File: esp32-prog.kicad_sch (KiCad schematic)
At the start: 14 parts

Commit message: draft schematics complete
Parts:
- added C7, C8, C9: 100n_0402_CL05B104KB54PNC, Capacitor_SMD:C_0603_1608Metric, symbol 00-kiml-capacitors-smd:100n_0402_CL05B104KB54PNC
- added D? (x3): 0603_RED_KT-0603R, LED_SMD:LED_0603_1608Metric, symbol 00-kiml-led-smd:0603_RED_KT-0603R
- added J?: 1.27mm_50mils_male_DW127R-22-10-23_02x05, Connector_PinHeader_1.27mm:PinHeader_2x05_P1.27mm_Vertical, symbol 00-kiml-connector-pin-header-1.27mm:1.27mm_50mils_male_DW127R-22-10-23_02x05
- added Q1, Q2: AO3400A, Package_TO_SOT_SMD:SOT-23, symbol 00-kiml-transitor-fet:AO3400A
- added R3, R4, R7, R8, R?: 10k_0402_0402WGF1002TCE, Resistor_SMD:R_0402_1005Metric, symbol 00-kiml-resistors-smd:10k_0402_0402WGF1002TCE
- added R5, R6, R? (x3): 1k_0402_0402WGF1001TCE, Resistor_SMD:R_0402_1005Metric, symbol 00-kiml-resistors-smd:1k_0402_0402WGF1001TCE
- added SW?: SW_DIP_x02_50mil_1.27mm_TP-02, symbol 00-kiml-button-switch-smd:SW_DIP_x02_50mil_1.27mm_TP-02
- added U5, U6, U?: 74LVC1G125GW_Nexperia, Package_TO_SOT_SMD:SOT-23-5, symbol 00-kiml-74xGxx:74LVC1G125GW_Nexperia
- R1, R2: renamed from R?; UserValue 1k -> 10k
- gave numbers to parts that had none: 12
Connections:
- net +5V: now also J?.1 (Pin_1), R?.1, SW?.4; no longer C1.1, L1.2, U1.3 (VI)
- net GND: now also J1.5 (GND), J1.6 (Shield), C7.2, C8.2, C9.2, D?.1 (K), D?.1 (K), D?.1 (K), J?.10 (Pin_10), J?.9 (Pin_9), R3.2, R4.2, R?.2, U5.3 (G), U6.3 (G), U?.3 (G); no longer U2.2 (VN), U2.4 (IO3), U2.6 (IO4)
- net TXD: now reaches U4.4
- net TXD: now also J?.8 (Pin_8)
- net at U3.13 (~{DTR}): now also U5.2
- net at U3.14 (~{RTS}): now also U6.2
- net at U3.3 (RXD): now also U?.4
- net +3V3 renamed +3.3VA
- net +3.3VA: now also SW?.2; no longer U4.5 (V)
- new net: Q1.2 (S), Q2.1 (G), R6.2, R8.2
- new net: R6.1, U6.4
- new net: D?.2 (A), R?.2 (x3)
- new net: R5.1, U5.4
- new net: Q1.1 (G), Q2.2 (S), R5.2, R7.2
- new net: R?.1, U?.1
- new net: R4.1, U6.1
- new net: R3.1, U5.1
- new net: U2.2 (VN), U2.4 (IO3), U2.6 (IO4)
- new net +3.3V: C7.1, C8.1, C9.1, J?.2 (Pin_2), R7.1, R8.1, R?.1, SW?.3, U4.5 (V), U5.5 (V), U6.5 (V), U?.5 (V)
- new net ESP_BOOT: J?.6 (Pin_6), Q2.3 (D)
- new net ESP_EN: J?.5 (Pin_5), Q1.3 (D)
- new net RXD: J?.7 (Pin_7), U?.2
- new net VBUS: C1.1, L1.2, R?.1, SW?.1, U1.3 (VI)
- no-connect marks 0 -> 6
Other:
- note added: "2. Mating wire should pair with https://www.tag-connect.com/product/tc2050-idc-nl-050-all"
- note added: "TODO: LEDs on TX/RX lines to indicate comms?"
- moved on the sheet: C1, C2, C3, C4, C5, C6, L1, R1, R2, U1, U2, U3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

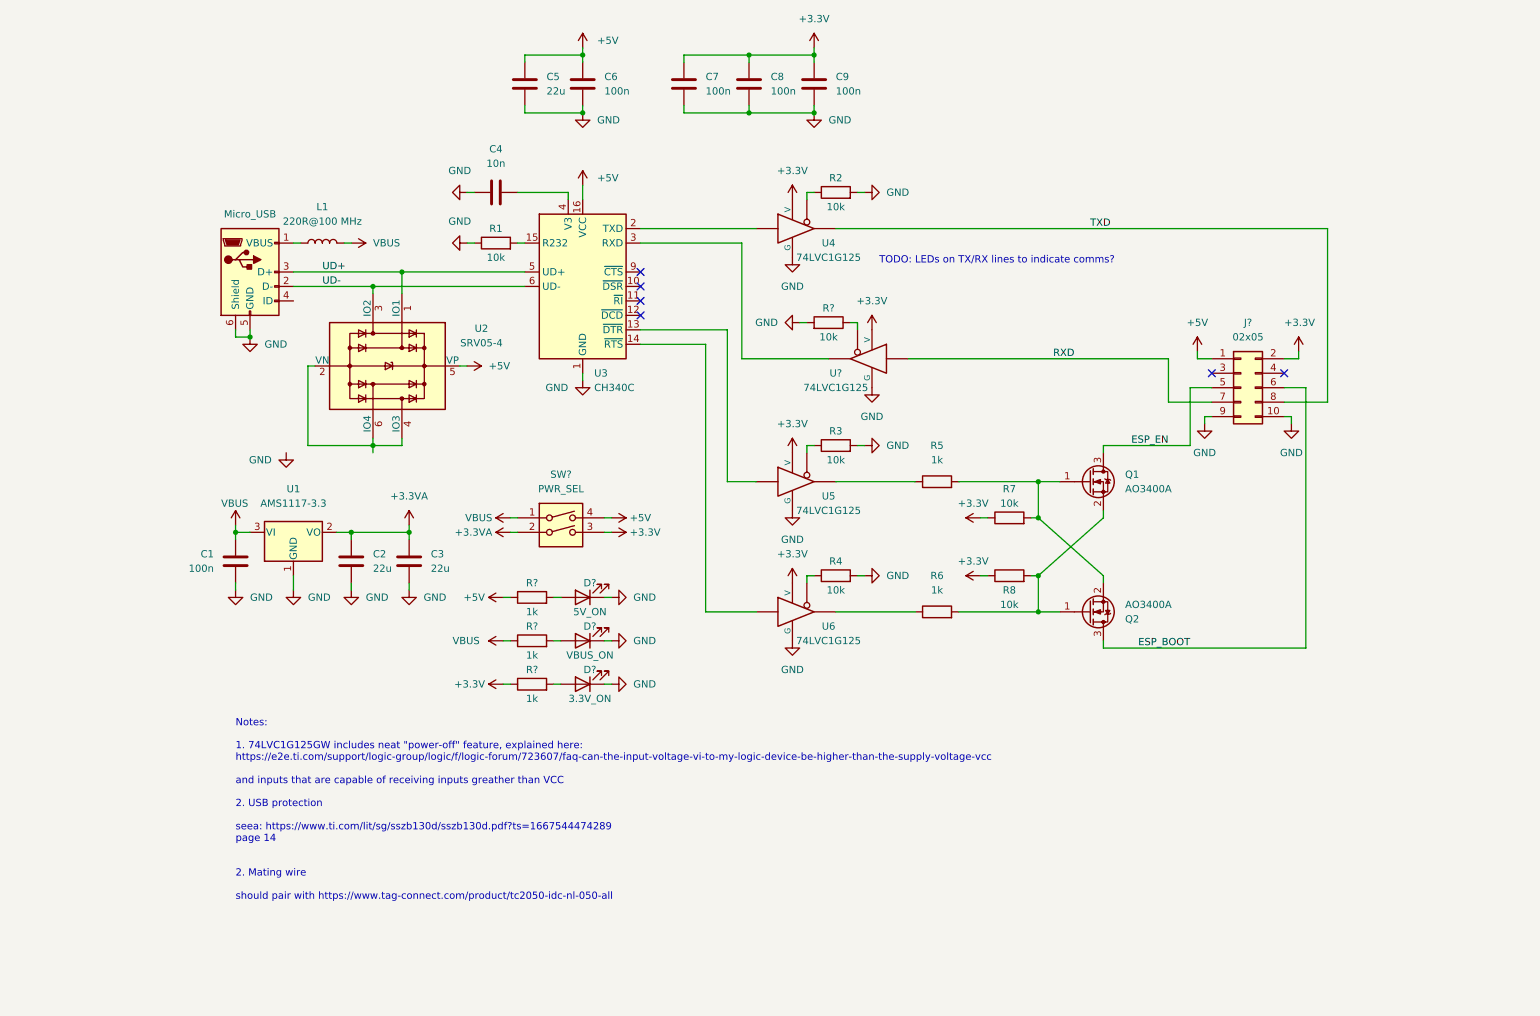
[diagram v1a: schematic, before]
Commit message: fix DRC in schematics
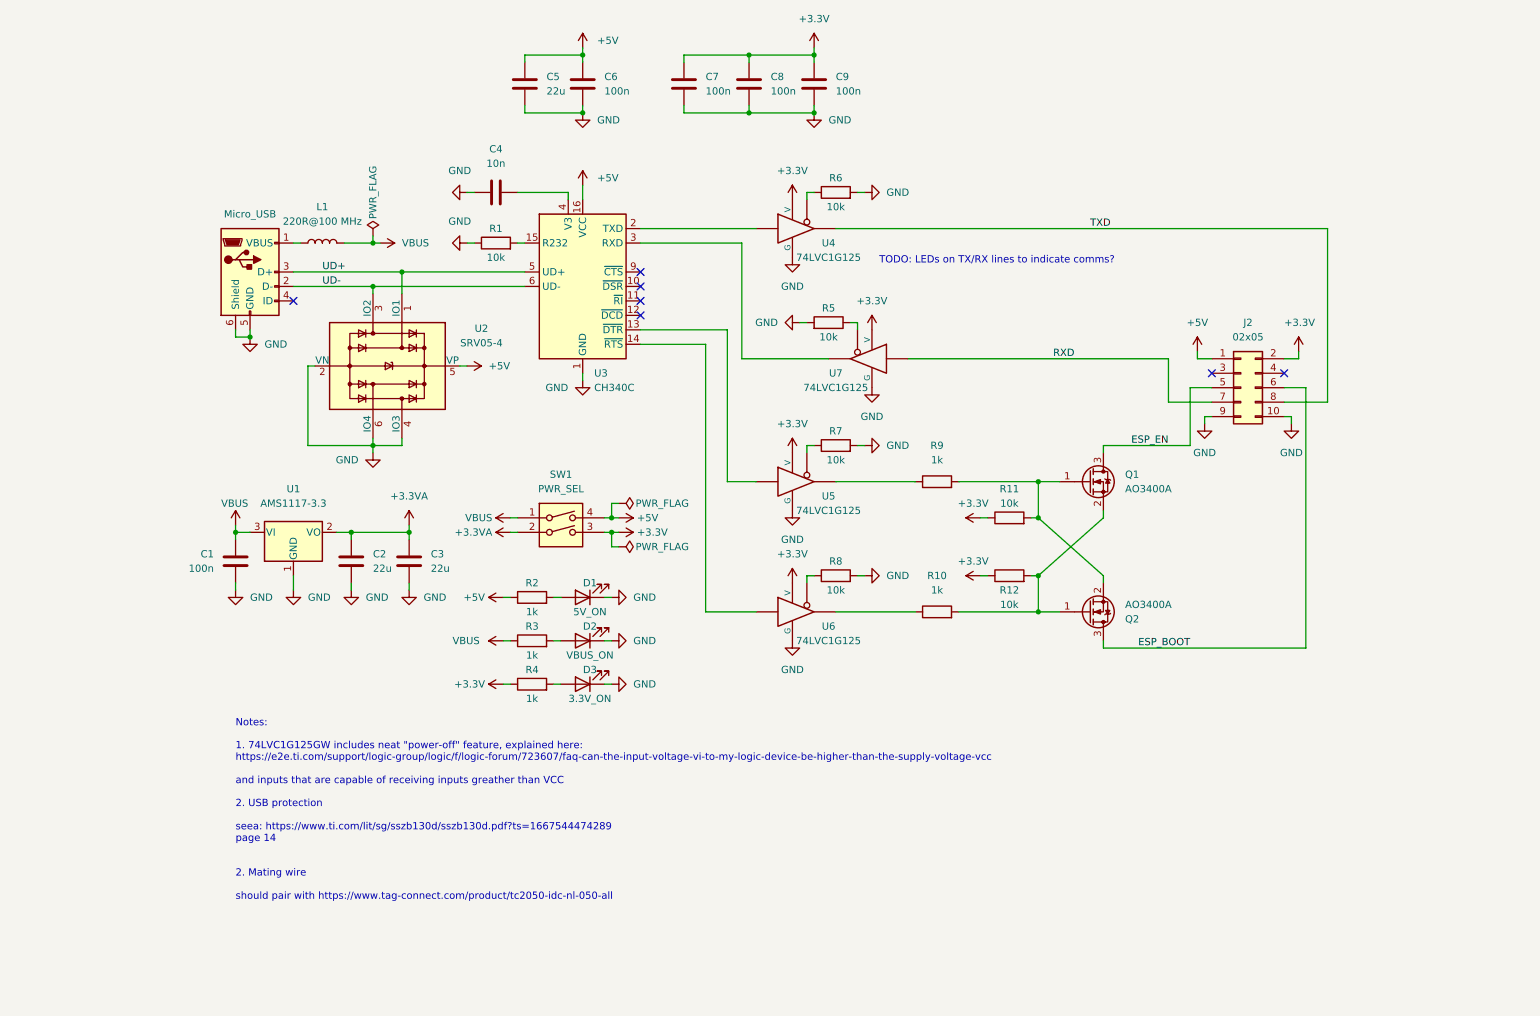
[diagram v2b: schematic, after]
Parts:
- SW1: renamed from SW?; footprint (none) -> 00-kiml-button-switch-smd:SW_DIP_1.27mm_0.50mil_TP-02
- gave numbers to parts that had none: 9
- renumbered R6 to R10, R7 to R11, R8 to R12, R2 to R6, R3 to R7, R4 to R8, R5 to R9
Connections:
- net GND: now also U2.2 (VN), U2.4 (IO3), U2.6 (IO4)
- no-connect marks 6 -> 7

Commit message: begin routing: place all basic blocks
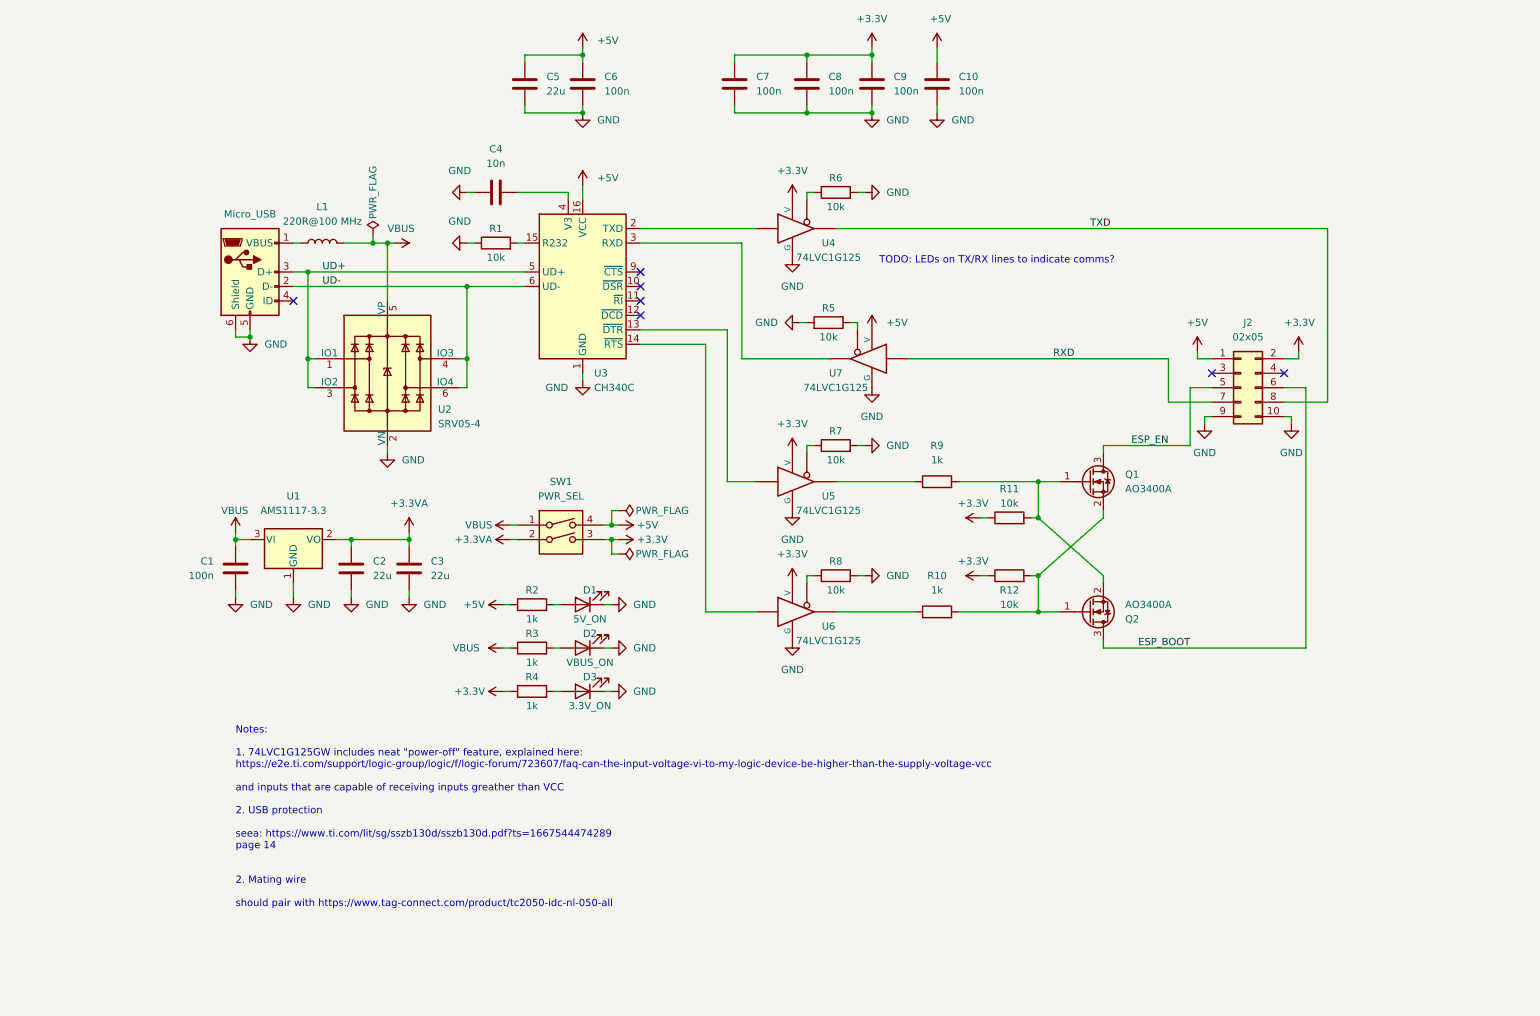
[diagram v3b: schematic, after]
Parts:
- added C7: 100n_0402_CL05B104KB54PNC, Capacitor_SMD:C_0603_1608Metric, symbol 00-kiml-capacitors-smd:100n_0402_CL05B104KB54PNC
- renumbered C9 to C10, C7 to C8, C8 to C9
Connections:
- net +3.3V: now also C7.1; no longer C10.1, U7.5 (V)
- net +5V: now also C10.1, U7.5 (V); no longer U2.5 (VP)
- net GND: now also C7.2; no longer U2.4 (IO3), U2.6 (IO4)
- net UD+: now also U2.3 (IO2)
- net UD-: now also U2.4 (IO3), U2.6 (IO4); no longer U2.3 (IO2)
- net VBUS: now also U2.5 (VP)
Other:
- company: (none) -> MAXLAB.IO INC.
- title: (none) -> ESP32 External Programmer
- moved on the sheet: C1, C10, C2, C3, C8, C9, D1, D2, D3, R2, R3, R4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

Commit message: draft route complete
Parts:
- added H1, H2, H3, H4: MH, MountingHole:MountingHole_3.2mm_M3_ISO7380_Pad, symbol Mechanical:MountingHole_Pad
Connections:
- net GND: now also J2.3 (Pin_3), J2.4 (Pin_4), H1.1, H2.1, H3.1, H4.1; no longer J1.6 (Shield), J2.10 (Pin_10), J2.9 (Pin_9)
- no-connect marks 7 -> 8

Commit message: draft route: complete, ready for review
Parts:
- J1: footprint Connector_USB:USB_Micro-B_Amphenol_10118194_Horizontal -> 00-kiml-connector-usb:USB_Micro-B_Amphenol_10118194_Horizontal
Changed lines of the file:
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@@
     (in_bom yes) (on_board yes) (fields_autoplaced)
     (property "Reference" "J1" (id 0) (at 58.42 54.61 0)
-      (effects (font (size 1.27 1.27)) (justify left) hide)
+      (effects (font (size 1.27 1.27)) (justify left))
     )
     (property "Value" "USB_B_Micro_10118194-0001LF" (id 1) (at 44.45 90.17 0)
       (effects (font (size 1.27 1.27)) (justify left) hide)
     )
-    (property "Footprint" "Connector_USB:USB_Micro-B_Amphenol_10118194_Horizontal" (id 2) (at 59.69 49.53 0)
+    (property "Footprint" "00-kiml-connector-usb:USB_Micro-B_Amphenol_10118194_Horizontal" (id 2) (at 59.69 49.53 0)
       (effects (font (size 1.27 1.27)) hide)
     )
@@
     )
     (path "/61903752-449a-430b-83a0-ed73de4efd4b"
-      (reference "J1") (unit 1) (value "USB_B_Micro_10118194-0001LF") (footprint "Connector_USB:USB_Micro-B_Amphenol_10118194_Horizontal")
+      (reference "J1") (unit 1) (value "USB_B_Micro_10118194-0001LF") (footprint "00-kiml-connector-usb:USB_Micro-B_Amphenol_10118194_Horizontal")
     )
     (path "/4aa1e128-d6c8-4313-a172-843969f07592"

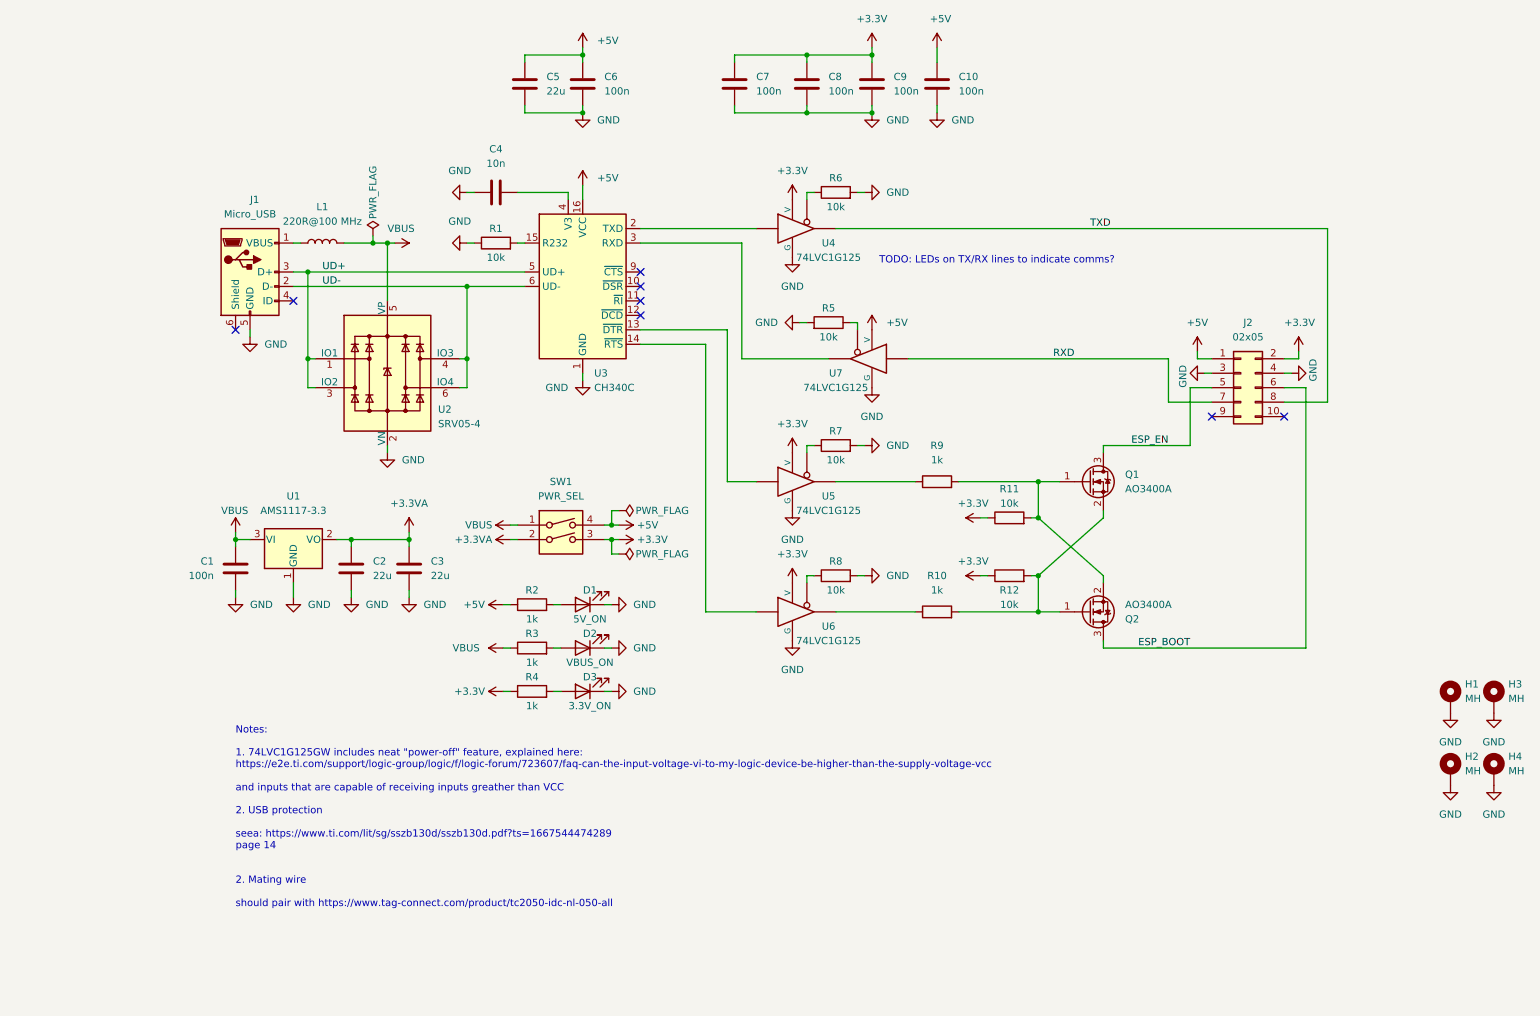
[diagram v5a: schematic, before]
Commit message: route: addressed R. comments w.r.t. power assign
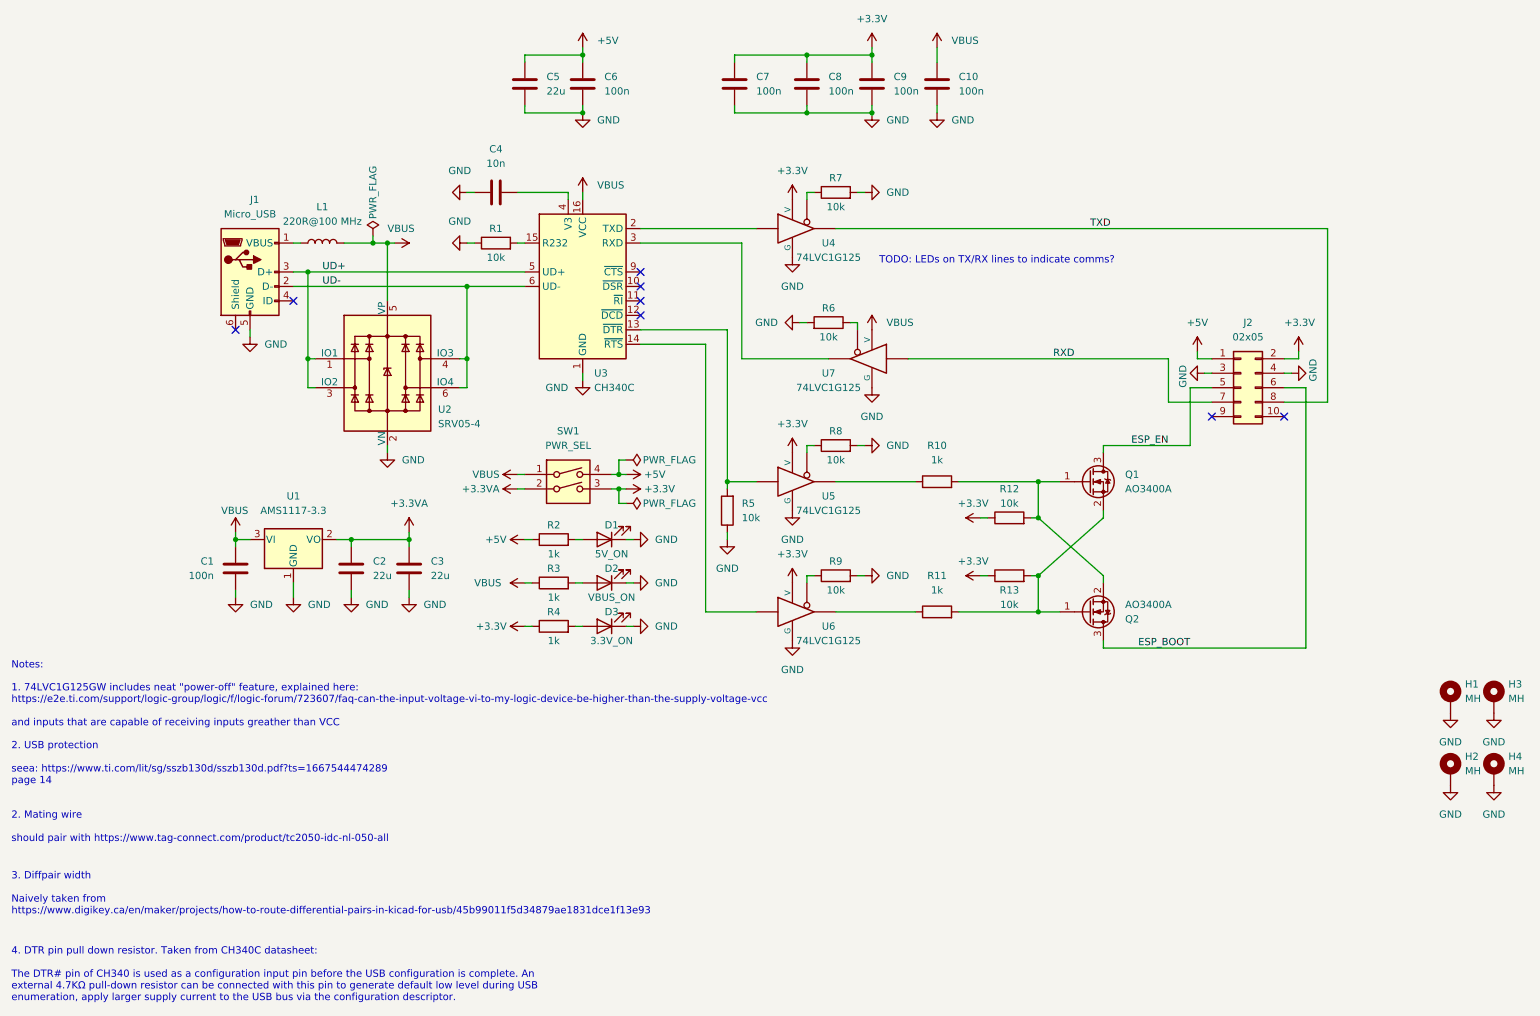
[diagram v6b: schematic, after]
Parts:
- added R5: 10k_0402_0402WGF1002TCE, Resistor_SMD:R_0402_1005Metric, symbol 00-kiml-resistors-smd:10k_0402_0402WGF1002TCE
- renumbered R9 to R10, R10 to R11, R11 to R12, R12 to R13, R5 to R6, R6 to R7, R7 to R8, R8 to R9
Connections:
- net +5V: no longer C10.1, U3.16 (VCC), U7.5 (V)
- net GND: now also R5.1
- net VBUS: now also C10.1, U3.16 (VCC), U7.5 (V)
- net at U3.13 (~{DTR}), U5.2: now also R5.2
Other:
- note added: "3. Diffpair width Naively taken from https://www.digikey.ca/en/maker/projects/how-to-route-differential-pairs-in-kicad-for-usb/45b99011f5d34879ae1831dce1f13e93"
- note added: "4. DTR pin pull down resistor. Taken from CH340C datasheet: The DTR# pin of CH340 is used as a configuration input pin before the USB configuration is complete. An external 4.7KΩ pull-down resistor can be connected with this pin to generate default low level during USB enumeration, apply larger supply current to the USB bus via the configuration descriptor."
- moved on the sheet: D1, D2, D3, R2, R3, R4, SW1

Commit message: fab: fix jlcpcb export - cpl file and such
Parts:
- R1, R10, R11, R12, R13, R2, R3, R4, R5, R6, R7, R8, R9: SBN1 Basic part -> (none); SNB1 (none) -> Basic part
- U3: symbol Interface_USB:CH340C -> 00-kiml-interface_usb:CH340C; LNK1 (none) -> https://jlcpcb.com/partdetail/wch_jiangsu_Qin_heng-CH340C/C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; MFR (none) -> WCH; MPN (none) -> CH340C; SNB1 (none) -> Extended part; SPL1 (none) -> JLCPCB; SPN1 (none) -> C84681; UserValue (none) -> CH340C
